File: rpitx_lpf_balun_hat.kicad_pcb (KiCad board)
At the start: 2 copper layers, 65 x 56 mm, 5 parts, among them P1 Conn_02x20_Odd_Even

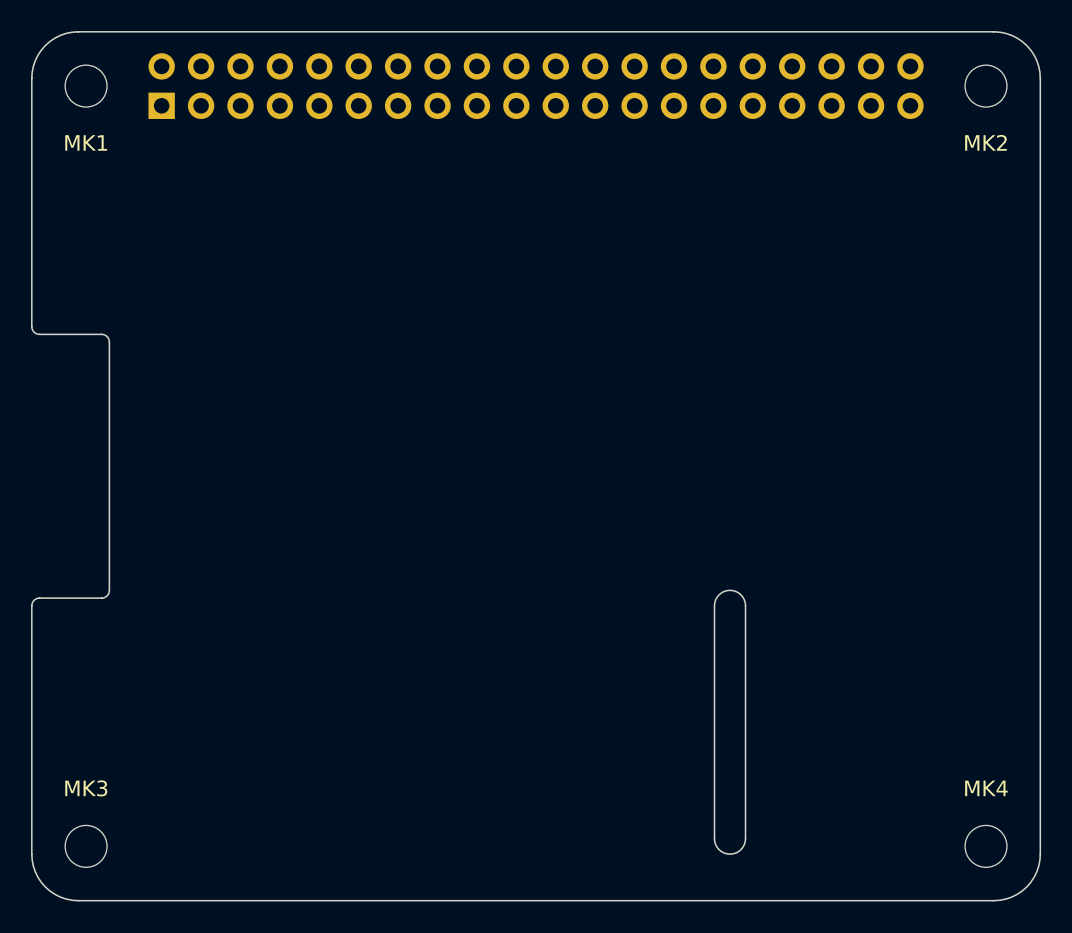
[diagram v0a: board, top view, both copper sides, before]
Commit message: Rough placement
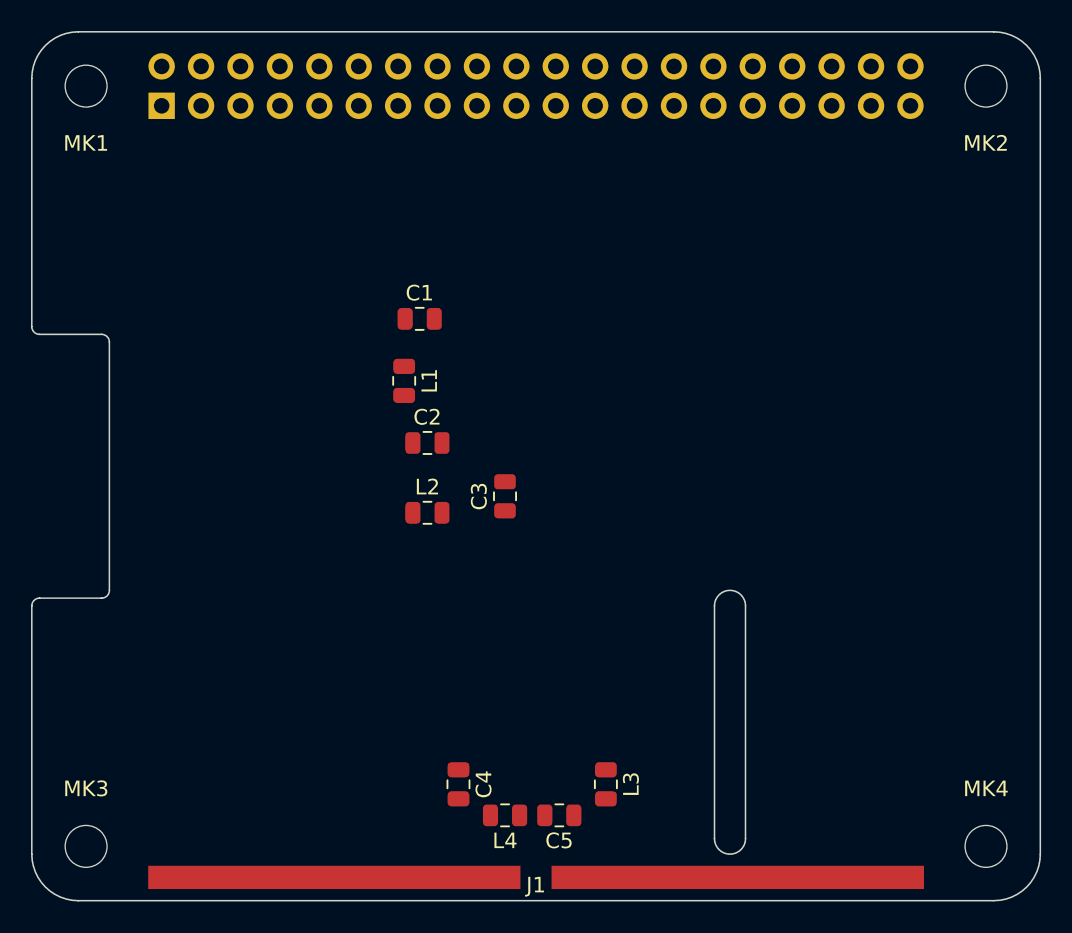
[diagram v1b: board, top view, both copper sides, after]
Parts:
- added C1: 5p9, Capacitor_SMD:C_0805_2012Metric, F.Cu at (225.0, 112.5)
- added C2: 10p2, Capacitor_SMD:C_0805_2012Metric, F.Cu at (225.5, 120.5)
- added C3: 5p9, Capacitor_SMD:C_0805_2012Metric, F.Cu at (230.5, 123.9)
- added C4: 8p95, Capacitor_SMD:C_0805_2012Metric, F.Cu at (227.5, 142.5)
- added C5: 8p95, Capacitor_SMD:C_0805_2012Metric, F.Cu at (234.0, 144.5)
- added J1: ANT, rpitx_lpf_balun_hat:rpitx_ant, F.Cu at (232.5, 148.5)
- added L1: 300n, Inductor_SMD:L_0805_2012Metric, F.Cu at (224.0, 116.5)
- added L2: 300n, Inductor_SMD:L_0805_2012Metric, F.Cu at (225.5, 125.0)
- added L3: 135n, Inductor_SMD:L_0805_2012Metric, F.Cu at (237.0, 142.5)
- added L4: 135n, Inductor_SMD:L_0805_2012Metric, F.Cu at (230.5, 144.5)
